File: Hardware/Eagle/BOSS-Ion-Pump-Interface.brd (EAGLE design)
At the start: 48.3 x 66 mm, 33 parts, among them J1 MOLEX-22112022, J2 MOLEX-22112042, J3 MOLEX-22112042, J4 MOLEX-22112062, U1 ISO224ADWVR, U2 ISO224ADWVR

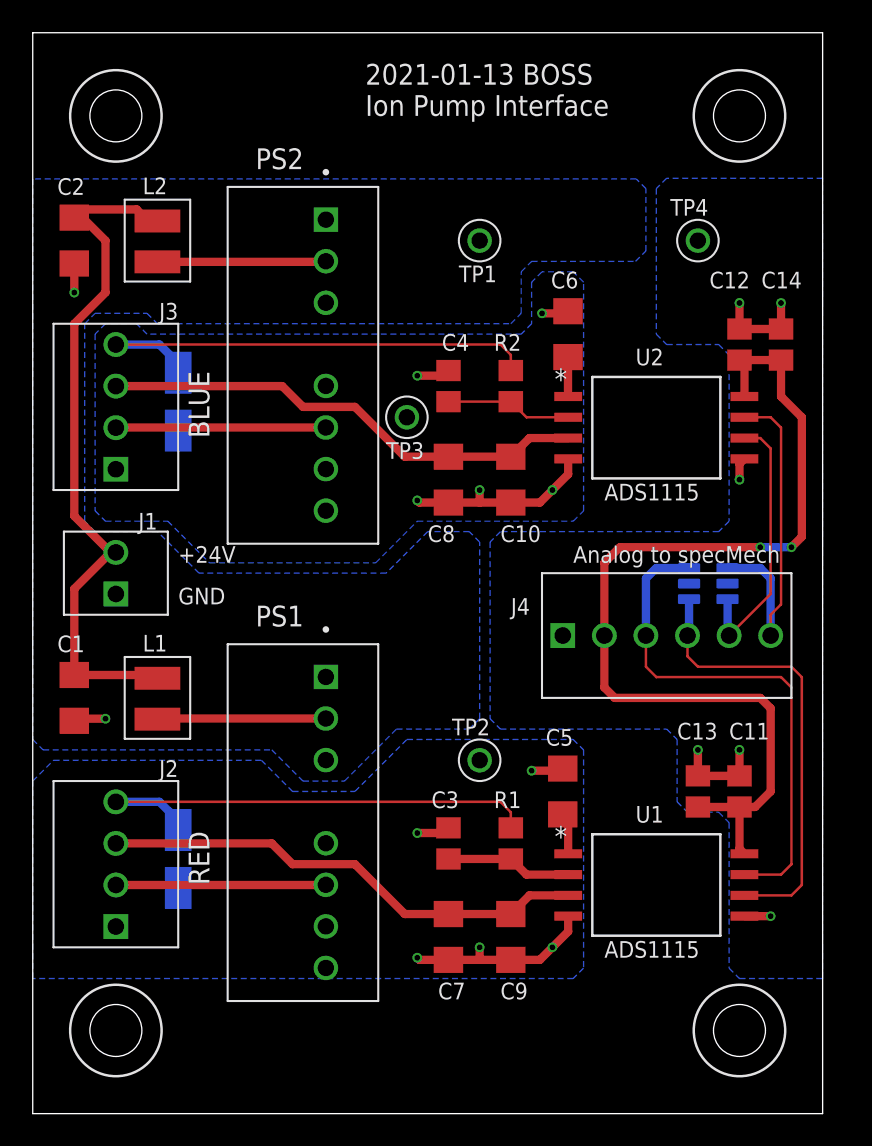
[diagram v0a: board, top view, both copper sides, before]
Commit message: Re-labeled nets, added 10uF filter on+5V in
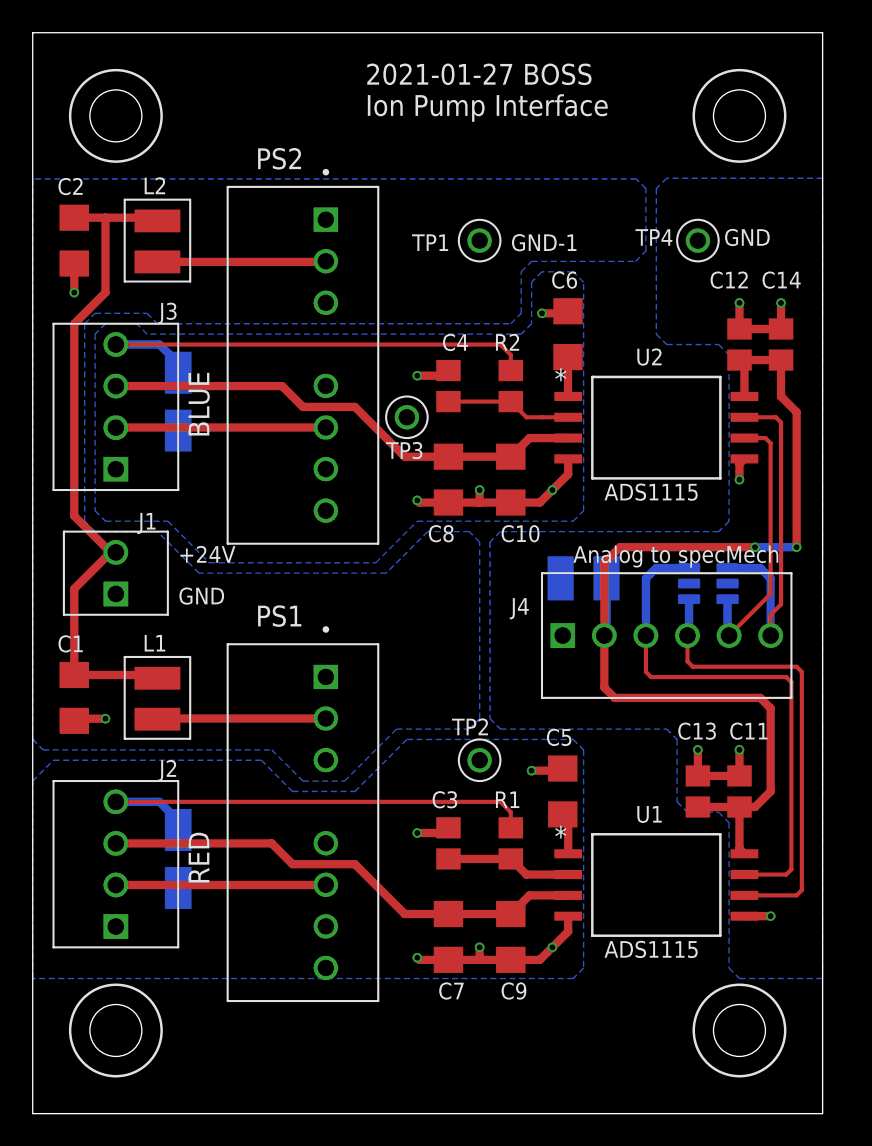
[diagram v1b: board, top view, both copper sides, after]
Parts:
- added C15: 10uF 50V, AUmlib:C1210
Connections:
- net +15V-BLUE renamed +15V-A
- net +15V-RED renamed +15V-B
- net +VIN-BLUE renamed +VIN-A
- net +VIN-RED renamed +VIN-B
- net FROM-BLUE-PUMP renamed FROM-PUMP-A
- net FROM-RED-PUMP renamed FROM-PUMP-B
- net GND-ISO-BLUE renamed GND-ISO-A
- net GND-ISO-RED renamed GND-ISO-B
- net IN-BLUE renamed IN-A
- net IN-RED renamed IN-B
- net OUTN-BLUE renamed OUTN-A
- net OUTN-RED renamed OUTN-B
- net OUTP-BLUE renamed OUTP-A
- net OUTP-RED renamed OUTP-B
- net VCAP-BLUE renamed VCAP-A
- net VCAP-RED renamed VCAP-B
- net VDD1-BLUE renamed VDD1-A
- net VDD1-RED renamed VDD1-B
- net +5V: now also C15.1
- net GND: now also C15.2
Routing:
- net +5V: track 60.1 -> 63.6 mm
- net +24V: track 42.7 -> 41.2 mm
- net OUTN-B: track 27.5 -> 28.1 mm
- net OUTP-B: track 31.6 -> 32.2 mm
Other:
- board text added: "2021-01-27 BOSS Ion Pump Interface"
- board text added: "GND-1"
- board text removed: "2021-01-13 BOSS Ion Pump Interface"
